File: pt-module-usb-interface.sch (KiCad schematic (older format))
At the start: 9 parts

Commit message: Connected EVERYTHING. Ran ERC. There are still some power errors.
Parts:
- 10k1: renamed from 10k; value R -> 10k1
- 27R1, 27R2: renamed from 27R; value R -> 27R
- 4k1: renamed from 4k7; value R -> 4k1
- gave numbers to parts that had none: 3
- renumbered 47pF to 47pF1, 47pF to 47pF2
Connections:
- no-connect marks 1 -> 5
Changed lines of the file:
@@
 LIBS:ftdi
 LIBS:relays
+LIBS:microchip_dspic33dsc
+LIBS:microchip_pic10mcu
+LIBS:microchip_pic12mcu
+LIBS:microchip_pic16mcu
+LIBS:microchip_pic18mcu
+LIBS:microchip_pic24mcu
+LIBS:microchip_pic32mcu
 LIBS:pt-module-cache
 EELAYER 25 0
@@
 $Descr A4 11693 8268
 encoding utf-8
-Sheet 8 13
+Sheet 7 13
 Title ""
 Date ""
@@
 $EndDescr
 $Comp
-L USB_OTG J?
+L USB_OTG J8
 U 1 1 59836C96
 P 3800 4850
-F 0 "J?" H 3600 5300 50  0000 L CNN
+F 0 "J8" H 3600 5300 50  0000 L CNN
 F 1 "USB_OTG" H 3600 5200 50  0000 L CNN
 F 2 "" H 3950 4800 50  0001 C CNN
@@
 $EndComp
 $Comp
-L R 4k7
+L R 4k1
 U 1 1 59836D8F
 P 5400 4900
-F 0 "4k7" V 5480 4900 50  0000 C CNN
-F 1 "R" V 5400 4900 50  0000 C CNN
+F 0 "4k1" V 5480 4900 50  0000 C CNN
+F 1 "4k1" V 5400 4900 50  0000 C CNN
 F 2 "" V 5330 4900 50  0001 C CNN
 F 3 "" H 5400 4900 50  0001 C CNN
@@
 $EndComp
 $Comp
-L R 10k
+L R 10k1
 U 1 1 59836DF0
 P 5400 5350
-F 0 "10k" V 5480 5350 50  0000 C CNN
-F 1 "R" V 5400 5350 50  0000 C CNN
+F 0 "10k1" V 5480 5350 50  0000 C CNN
+F 1 "10k1" V 5400 5350 50  0000 C CNN
 F 2 "" V 5330 5350 50  0001 C CNN
 F 3 "" H 5400 5350 50  0001 C CNN
@@
 $EndComp
 $Comp
-L GND #PWR055
+L GND #PWR062
 U 1 1 59837539
 P 5400 5650
-F 0 "#PWR055" H 5400 5400 50  0001 C CNN
+F 0 "#PWR062" H 5400 5400 50  0001 C CNN
 F 1 "GND" H 5400 5500 50  0000 C CNN
 F 2 "" H 5400 5650 50  0001 C CNN
@@
 $EndComp
 $Comp
-L GND #PWR056
+L GND #PWR063
 U 1 1 59837659
 P 3800 5400
-F 0 "#PWR056" H 3800 5150 50  0001 C CNN
+F 0 "#PWR063" H 3800 5150 50  0001 C CNN
 F 1 "GND" H 3800 5250 50  0000 C CNN
 F 2 "" H 3800 5400 50  0001 C CNN
@@
 NoConn ~ 4100 5050
 $Comp
-L +3.3V #PWR057
+L +3.3V #PWR064
 U 1 1 59837A65
 P 5650 1750
-F 0 "#PWR057" H 5650 1600 50  0001 C CNN
+F 0 "#PWR064" H 5650 1600 50  0001 C CNN
 F 1 "+3.3V" H 5650 1890 50  0000 C CNN
 F 2 "" H 5650 1750 50  0001 C CNN
@@
 $EndComp
 $Comp
-L R 27R
+L R 27R1
 U 1 1 59837D1B
 P 4700 2650
-F 0 "27R" V 4780 2650 50  0000 C CNN
-F 1 "R" V 4700 2650 50  0000 C CNN
+F 0 "27R1" V 4780 2650 50  0000 C CNN
+F 1 "27R" V 4700 2650 50  0000 C CNN
 F 2 "" V 4630 2650 50  0001 C CNN
 F 3 "" H 4700 2650 50  0001 C CNN
@@
 $EndComp
 $Comp
-L R 27R
+L R 27R2
 U 1 1 59838172
 P 4700 2750
-F 0 "27R" V 4780 2750 50  0000 C CNN
-F 1 "R" V 4700 2750 50  0000 C CNN
+F 0 "27R2" V 4780 2750 50  0000 C CNN
+F 1 "27R" V 4700 2750 50  0000 C CNN
 F 2 "" V 4630 2750 50  0001 C CNN
 F 3 "" H 4700 2750 50  0001 C CNN
@@
 $EndComp
 $Comp
-L C_Small 47pF
+L C_Small 47pF1
 U 1 1 59838B31
 P 4700 3450
-F 0 "47pF" H 4710 3520 50  0000 L CNN
+F 0 "47pF1" H 4710 3520 50  0000 L CNN
 F 1 "C_Small" H 4710 3370 50  0000 L CNN
 F 2 "" H 4700 3450 50  0001 C CNN
@@
 $EndComp
 $Comp
-L C_Small 47pF
+L C_Small 47pF2
 U 1 1 59838B9F
 P 4700 3750
-F 0 "47pF" H 4710 3820 50  0000 L CNN
+F 0 "47pF2" H 4710 3820 50  0000 L CNN
 F 1 "C_Small" H 4710 3670 50  0000 L CNN
 F 2 "" H 4700 3750 50  0001 C CNN
@@
 $EndComp
 $Comp
-L GND #PWR058
+L GND #PWR065
 U 1 1 59838D4F
 P 4800 3600
-F 0 "#PWR058" H 4800 3350 50  0001 C CNN
+F 0 "#PWR065" H 4800 3350 50  0001 C CNN
 F 1 "GND" H 4800 3450 50  0000 C CNN
 F 2 "" H 4800 3600 50  0001 C CNN
@@
 $EndComp
 $Comp
-L FT230XS U?
+L FT230XS U8
 U 1 1 59839565
 P 5750 2750
-F 0 "U?" H 5200 3350 50  0000 L CNN
+F 0 "U8" H 5200 3350 50  0000 L CNN
 F 1 "FT230XS" H 6050 3350 50  0000 L CNN
 F 2 "SSOP-16" H 5750 2750 50  0001 C CNN
@@
 $EndComp
 $Comp
-L C_Small C?
+L C_Small C13
 U 1 1 59839A23
 P 4950 3200
-F 0 "C?" H 4960 3270 50  0000 L CNN
+F 0 "C13" H 4960 3270 50  0000 L CNN
 F 1 "C_Small" H 4960 3120 50  0000 L CNN
 F 2 "" H 4950 3200 50  0001 C CNN
@@
 	1    0    0    -1
 $EndComp
-Wire Wire Line
-	5400 5500 5400 5650
-Wire Wire Line
-	3800 5250 3800 5400
-Wire Wire Line
-	5650 1750 5650 2050
-Wire Wire Line
-	5050 2650 4850 2650
-Wire Wire Line
-	5050 2750 4850 2750
-Wire Wire Line
-	4100 4950 4300 4950
-Wire Wire Line
-	4300 4950 4300 2650
-Wire Wire Line
-	4300 2650 4550 2650
-Wire Wire Line
-	4100 4850 4450 4850
-Wire Wire Line
-	4450 4850 4450 2750
-Wire Wire Line
-	4450 2750 4550 2750
-Wire Wire Line
-	4600 3450 4300 3450
-Connection ~ 4300 3450
-Wire Wire Line
-	4600 3750 4450 3750
-Connection ~ 4450 3750
-Wire Wire Line
-	4800 3450 4800 3750
-Connection ~ 4800 3600
-Wire Wire Line
-	4950 1950 5850 1950
-Wire Wire Line
-	4950 1950 4950 3100
-Wire Wire Line
-	4950 2350 5050 2350
-Wire Wire Line
-	4950 2950 5050 2950
-Connection ~ 4950 2350
-Wire Wire Line
-	5850 1950 5850 2050
-Wire Wire Line
-	6450 2850 6550 2850
-Wire Wire Line
-	6550 2850 6550 5150
-Connection ~ 4950 2950
-Wire Wire Line
-	4950 3300 4950 3500
-Wire Wire Line
-	4950 3500 5850 3500
-Wire Wire Line
-	5650 3500 5650 3450
-Wire Wire Line
-	5850 3500 5850 3450
-Connection ~ 5650 3500
-$Comp
-L GND #PWR059
+$Comp
+L GND #PWR066
 U 1 1 59839F17
 P 5650 3500
-F 0 "#PWR059" H 5650 3250 50  0001 C CNN
+F 0 "#PWR066" H 5650 3250 50  0001 C CNN
 F 1 "GND" H 5650 3350 50  0000 C CNN
 F 2 "" H 5650 3500 50  0001 C CNN
@@
 	1    0    0    -1
 $EndComp
-Wire Wire Line
-	5400 4750 5400 4650
-Wire Wire Line
-	5400 5200 5400 5050
 Text HLabel 6450 2350 2    60   Input ~ 0
 USB_UART_TXD
@@
 Text HLabel 6450 2650 2    60   Input ~ 0
 USB_UART_CTS
+NoConn ~ 6450 2950
+NoConn ~ 6450 3050
+NoConn ~ 6450 3150
+Wire Wire Line
+	5400 5500 5400 5650
+Wire Wire Line
+	3800 5250 3800 5400
+Wire Wire Line
+	5650 1750 5650 2050
+Wire Wire Line
+	5050 2650 4850 2650
+Wire Wire Line
+	5050 2750 4850 2750
+Wire Wire Line
+	4100 4950 4300 4950
+Wire Wire Line
+	4300 4950 4300 2650
+Wire Wire Line
+	4300 2650 4550 2650
+Wire Wire Line
+	4100 4850 4450 4850
+Wire Wire Line
+	4450 4850 4450 2750
+Wire Wire Line
+	4450 2750 4550 2750
+Wire Wire Line
+	4600 3450 4300 3450
+Connection ~ 4300 3450
+Wire Wire Line
+	4600 3750 4450 3750
+Connection ~ 4450 3750
+Wire Wire Line
+	4800 3450 4800 3750
+Connection ~ 4800 3600
+Wire Wire Line
+	4950 1950 5850 1950
+Wire Wire Line
+	4950 1950 4950 3100
+Wire Wire Line
+	4950 2350 5050 2350
+Wire Wire Line
+	4950 2950 5050 2950
+Connection ~ 4950 2350
+Wire Wire Line
+	5850 1950 5850 2050
+Wire Wire Line
+	6450 2850 6550 2850
+Wire Wire Line
+	6550 2850 6550 5150
+Connection ~ 4950 2950
+Wire Wire Line
+	4950 3300 4950 3500
+Wire Wire Line
+	4950 3500 5850 3500
+Wire Wire Line
+	5650 3500 5650 3450
+Wire Wire Line
+	5850 3500 5850 3450
+Connection ~ 5650 3500
+Wire Wire Line
+	5400 4750 5400 4650
+Wire Wire Line
+	5400 5200 5400 5050
 Wire Wire Line
 	5400 4650 4100 4650
@@
 Connection ~ 5400 5150
 Connection ~ 5650 1950
+NoConn ~ 3700 5250
 $EndSCHEMATC

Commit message: USB interface fix
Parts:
- C13: renamed from 47pF1; value C_Small -> 47pF
- C14: renamed from 47pF2; value C_Small -> 47pF
- C15: renamed from C13; value C_Small -> 100nF
- R17: renamed from 4k1; value 4k1 -> 4k7
- R18: renamed from 10k1; value 10k1 -> 10k
- renumbered 27R1 to R15, 27R2 to R16
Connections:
- net +3V3: no longer C15.1, U8.10 (3V3OUT), U8.11 (~RESET), U8.3 (VCCIO)
- net at J8.1 (VBUS): now also R17.2; no longer R17.1
- net at C13.2, J8.2 (D-): now also R15.1; no longer R15.2
- net at C14.2, J8.3 (D+): now also R16.1; no longer R16.2
- net at R18.1, U8.15 (CBUS0): now also R17.1; no longer R17.2
- net at U8.9 (USBDM): now also R15.2; no longer R15.1
- net at U8.8 (USBDP): now also R16.2; no longer R16.1
- new net: C15.1, U8.10 (3V3OUT), U8.11 (~RESET), U8.3 (VCCIO)
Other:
- moved on the sheet: J8, R15, R16, R17, R18
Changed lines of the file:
@@
 L USB_OTG J8
 U 1 1 59836C96
-P 3800 4850
-F 0 "J8" H 3600 5300 50  0000 L CNN
-F 1 "USB_OTG" H 3600 5200 50  0000 L CNN
-F 2 "" H 3950 4800 50  0001 C CNN
-F 3 "" H 3950 4800 50  0001 C CNN
-	1    3800 4850
-	1    0    0    -1
-$EndComp
-$Comp
-L R 4k1
+P 3800 4200
+F 0 "J8" H 3600 4650 50  0000 L CNN
+F 1 "USB_OTG" H 3600 4550 50  0000 L CNN
+F 2 "" H 3950 4150 50  0001 C CNN
+F 3 "" H 3950 4150 50  0001 C CNN
+	1    3800 4200
+	1    0    0    -1
+$EndComp
+$Comp
+L R R17
 U 1 1 59836D8F
-P 5400 4900
-F 0 "4k1" V 5480 4900 50  0000 C CNN
-F 1 "4k1" V 5400 4900 50  0000 C CNN
-F 2 "" V 5330 4900 50  0001 C CNN
-F 3 "" H 5400 4900 50  0001 C CNN
-	1    5400 4900
-	1    0    0    -1
-$EndComp
-$Comp
-L R 10k1
+P 5600 4000
+F 0 "R17" V 5680 4000 50  0000 C CNN
+F 1 "4k7" V 5600 4000 50  0000 C CNN
+F 2 "" V 5530 4000 50  0001 C CNN
+F 3 "" H 5600 4000 50  0001 C CNN
+	1    5600 4000
+	0    1    1    0
+$EndComp
+$Comp
+L R R18
 U 1 1 59836DF0
-P 5400 5350
-F 0 "10k1" V 5480 5350 50  0000 C CNN
-F 1 "10k1" V 5400 5350 50  0000 C CNN
-F 2 "" V 5330 5350 50  0001 C CNN
-F 3 "" H 5400 5350 50  0001 C CNN
-	1    5400 5350
-	1    0    0    -1
-$EndComp
-$Comp
-L GND #PWR062
+P 5900 4200
+F 0 "R18" V 5980 4200 50  0000 C CNN
+F 1 "10k" V 5900 4200 50  0000 C CNN
+F 2 "" V 5830 4200 50  0001 C CNN
+F 3 "" H 5900 4200 50  0001 C CNN
+	1    5900 4200
+	1    0    0    -1
+$EndComp
+$Comp
+L GND #PWR62
 U 1 1 59837539
-P 5400 5650
-F 0 "#PWR062" H 5400 5400 50  0001 C CNN
-F 1 "GND" H 5400 5500 50  0000 C CNN
-F 2 "" H 5400 5650 50  0001 C CNN
-F 3 "" H 5400 5650 50  0001 C CNN
-	1    5400 5650
-	1    0    0    -1
-$EndComp
-$Comp
-L GND #PWR063
+P 5900 4500
+F 0 "#PWR62" H 5900 4250 50  0001 C CNN
+F 1 "GND" H 5900 4350 50  0000 C CNN
+F 2 "" H 5900 4500 50  0001 C CNN
+F 3 "" H 5900 4500 50  0001 C CNN
+	1    5900 4500
+	1    0    0    -1
+$EndComp
+$Comp
+L GND #PWR58
 U 1 1 59837659
-P 3800 5400
-F 0 "#PWR063" H 3800 5150 50  0001 C CNN
-F 1 "GND" H 3800 5250 50  0000 C CNN
-F 2 "" H 3800 5400 50  0001 C CNN
-F 3 "" H 3800 5400 50  0001 C CNN
-	1    3800 5400
-	1    0    0    -1
-$EndComp
-NoConn ~ 4100 5050
-$Comp
-L +3.3V #PWR064
+P 3800 4750
+F 0 "#PWR58" H 3800 4500 50  0001 C CNN
+F 1 "GND" H 3800 4600 50  0000 C CNN
+F 2 "" H 3800 4750 50  0001 C CNN
+F 3 "" H 3800 4750 50  0001 C CNN
+	1    3800 4750
+	1    0    0    -1
+$EndComp
+NoConn ~ 4100 4400
+$Comp
+L +3.3V #PWR60
 U 1 1 59837A65
 P 5650 1750
-F 0 "#PWR064" H 5650 1600 50  0001 C CNN
+F 0 "#PWR60" H 5650 1600 50  0001 C CNN
 F 1 "+3.3V" H 5650 1890 50  0000 C CNN
 F 2 "" H 5650 1750 50  0001 C CNN
@@
 $EndComp
 $Comp
-L R 27R1
+L R R15
 U 1 1 59837D1B
-P 4700 2650
-F 0 "27R1" V 4780 2650 50  0000 C CNN
-F 1 "27R" V 4700 2650 50  0000 C CNN
-F 2 "" V 4630 2650 50  0001 C CNN
-F 3 "" H 4700 2650 50  0001 C CNN
-	1    4700 2650
-	0    1    1    0
-$EndComp
-$Comp
-L R 27R2
+P 4300 3000
+F 0 "R15" V 4380 3000 50  0000 C CNN
+F 1 "27R" V 4300 3000 50  0000 C CNN
+F 2 "" V 4230 3000 50  0001 C CNN
+F 3 "" H 4300 3000 50  0001 C CNN
+	1    4300 3000
+	-1   0    0    1
+$EndComp
+$Comp
+L R R16
 U 1 1 59838172
-P 4700 2750
-F 0 "27R2" V 4780 2750 50  0000 C CNN
-F 1 "27R" V 4700 2750 50  0000 C CNN
-F 2 "" V 4630 2750 50  0001 C CNN
-F 3 "" H 4700 2750 50  0001 C CNN
-	1    4700 2750
-	0    1    1    0
-$EndComp
-$Comp
-L C_Small 47pF1
+P 4500 3000
+F 0 "R16" V 4580 3000 50  0000 C CNN
+F 1 "27R" V 4500 3000 50  0000 C CNN
+F 2 "" V 4430 3000 50  0001 C CNN
+F 3 "" H 4500 3000 50  0001 C CNN
+	1    4500 3000
+	-1   0    0    1
+$EndComp
+$Comp
+L C_Small C13
 U 1 1 59838B31
 P 4700 3450
-F 0 "47pF1" H 4710 3520 50  0000 L CNN
-F 1 "C_Small" H 4710 3370 50  0000 L CNN
+F 0 "C13" H 4710 3520 50  0000 L CNN
+F 1 "47pF" H 4710 3370 50  0000 L CNN
 F 2 "" H 4700 3450 50  0001 C CNN
 F 3 "" H 4700 3450 50  0001 C CNN
@@
 $EndComp
 $Comp
-L C_Small 47pF2
+L C_Small C14
 U 1 1 59838B9F
 P 4700 3750
-F 0 "47pF2" H 4710 3820 50  0000 L CNN
-F 1 "C_Small" H 4710 3670 50  0000 L CNN
+F 0 "C14" H 4710 3820 50  0000 L CNN
+F 1 "47pF" H 4710 3670 50  0000 L CNN
 F 2 "" H 4700 3750 50  0001 C CNN
 F 3 "" H 4700 3750 50  0001 C CNN
@@
 $EndComp
 $Comp
-L GND #PWR065
+L GND #PWR59
 U 1 1 59838D4F
 P 4800 3600
-F 0 "#PWR065" H 4800 3350 50  0001 C CNN
+F 0 "#PWR59" H 4800 3350 50  0001 C CNN
 F 1 "GND" H 4800 3450 50  0000 C CNN
 F 2 "" H 4800 3600 50  0001 C CNN
@@
 $EndComp
 $Comp
-L C_Small C13
+L C_Small C15
 U 1 1 59839A23
 P 4950 3200
-F 0 "C13" H 4960 3270 50  0000 L CNN
-F 1 "C_Small" H 4960 3120 50  0000 L CNN
+F 0 "C15" H 4960 3270 50  0000 L CNN
+F 1 "100nF" H 4960 3120 50  0000 L CNN
 F 2 "" H 4950 3200 50  0001 C CNN
 F 3 "" H 4950 3200 50  0001 C CNN
@@
 $EndComp
 $Comp
-L GND #PWR066
+L GND #PWR61
 U 1 1 59839F17
 P 5650 3500
-F 0 "#PWR066" H 5650 3250 50  0001 C CNN
+F 0 "#PWR61" H 5650 3250 50  0001 C CNN
 F 1 "GND" H 5650 3350 50  0000 C CNN
 F 2 "" H 5650 3500 50  0001 C CNN
@@
 NoConn ~ 6450 3050
 NoConn ~ 6450 3150
-Wire Wire Line
-	5400 5500 5400 5650
-Wire Wire Line
-	3800 5250 3800 5400
-Wire Wire Line
-	5650 1750 5650 2050
-Wire Wire Line
-	5050 2650 4850 2650
-Wire Wire Line
-	5050 2750 4850 2750
-Wire Wire Line
-	4100 4950 4300 4950
-Wire Wire Line
-	4300 4950 4300 2650
-Wire Wire Line
-	4300 2650 4550 2650
-Wire Wire Line
-	4100 4850 4450 4850
-Wire Wire Line
-	4450 4850 4450 2750
-Wire Wire Line
-	4450 2750 4550 2750
-Wire Wire Line
-	4600 3450 4300 3450
-Connection ~ 4300 3450
-Wire Wire Line
-	4600 3750 4450 3750
-Connection ~ 4450 3750
+NoConn ~ 3700 4600
+Wire Wire Line
+	5900 4350 5900 4500
+Wire Wire Line
+	3800 4600 3800 4750
+Wire Wire Line
+	4500 2750 5050 2750
+Wire Wire Line
+	4500 4200 4100 4200
 Wire Wire Line
 	4800 3450 4800 3750
@@
 Wire Wire Line
 	6450 2850 6550 2850
-Wire Wire Line
-	6550 2850 6550 5150
 Connection ~ 4950 2950
 Wire Wire Line
@@
 Connection ~ 5650 3500
 Wire Wire Line
-	5400 4750 5400 4650
-Wire Wire Line
-	5400 5200 5400 5050
-Wire Wire Line
-	5400 4650 4100 4650
-Wire Wire Line
-	6550 5150 5400 5150
-Connection ~ 5400 5150
-Connection ~ 5650 1950
-NoConn ~ 3700 5250
+	4100 4000 5450 4000
+Wire Wire Line
+	5650 2050 5650 1750
+Wire Wire Line
+	6550 2850 6550 4000
+Wire Wire Line
+	6550 4000 5750 4000
+Wire Wire Line
+	5900 4050 5900 4000
+Connection ~ 5900 4000
+Wire Wire Line
+	4300 4300 4100 4300
+Wire Wire Line
+	4500 2750 4500 2850
+Wire Wire Line
+	4500 3150 4500 4200
+Connection ~ 4500 3750
+Wire Wire Line
+	4600 3750 4500 3750
+Wire Wire Line
+	5050 2650 4300 2650
+Wire Wire Line
+	4300 2650 4300 2850
+Wire Wire Line
+	4300 3150 4300 4300
+Wire Wire Line
+	4300 3450 4600 3450
+Connection ~ 4300 3450
 $EndSCHEMATC

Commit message: Re-annotation
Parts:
- renumbered C13 to C11, C14 to C12, C15 to C13, R15 to R13, R16 to R14, R17 to R15, R18 to R16, U8 to U7
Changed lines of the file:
@@
 $EndComp
 $Comp
-L R R17
+L R R15
 U 1 1 59836D8F
 P 5600 4000
-F 0 "R17" V 5680 4000 50  0000 C CNN
+F 0 "R15" V 5680 4000 50  0000 C CNN
 F 1 "4k7" V 5600 4000 50  0000 C CNN
 F 2 "" V 5530 4000 50  0001 C CNN
@@
 $EndComp
 $Comp
-L R R18
+L R R16
 U 1 1 59836DF0
 P 5900 4200
-F 0 "R18" V 5980 4200 50  0000 C CNN
+F 0 "R16" V 5980 4200 50  0000 C CNN
 F 1 "10k" V 5900 4200 50  0000 C CNN
 F 2 "" V 5830 4200 50  0001 C CNN
@@
 $EndComp
 $Comp
-L GND #PWR62
+L GND #PWR59
 U 1 1 59837539
 P 5900 4500
-F 0 "#PWR62" H 5900 4250 50  0001 C CNN
+F 0 "#PWR59" H 5900 4250 50  0001 C CNN
 F 1 "GND" H 5900 4350 50  0000 C CNN
 F 2 "" H 5900 4500 50  0001 C CNN
@@
 $EndComp
 $Comp
-L GND #PWR58
+L GND #PWR55
 U 1 1 59837659
 P 3800 4750
-F 0 "#PWR58" H 3800 4500 50  0001 C CNN
+F 0 "#PWR55" H 3800 4500 50  0001 C CNN
 F 1 "GND" H 3800 4600 50  0000 C CNN
 F 2 "" H 3800 4750 50  0001 C CNN
@@
 NoConn ~ 4100 4400
 $Comp
-L +3.3V #PWR60
+L +3.3V #PWR57
 U 1 1 59837A65
 P 5650 1750
-F 0 "#PWR60" H 5650 1600 50  0001 C CNN
+F 0 "#PWR57" H 5650 1600 50  0001 C CNN
 F 1 "+3.3V" H 5650 1890 50  0000 C CNN
 F 2 "" H 5650 1750 50  0001 C CNN
@@
 $EndComp
 $Comp
-L R R15
+L R R13
 U 1 1 59837D1B
 P 4300 3000
-F 0 "R15" V 4380 3000 50  0000 C CNN
+F 0 "R13" V 4380 3000 50  0000 C CNN
 F 1 "27R" V 4300 3000 50  0000 C CNN
 F 2 "" V 4230 3000 50  0001 C CNN
@@
 $EndComp
 $Comp
-L R R16
+L R R14
 U 1 1 59838172
 P 4500 3000
-F 0 "R16" V 4580 3000 50  0000 C CNN
+F 0 "R14" V 4580 3000 50  0000 C CNN
 F 1 "27R" V 4500 3000 50  0000 C CNN
 F 2 "" V 4430 3000 50  0001 C CNN
@@
 $EndComp
 $Comp
-L C_Small C13
+L C_Small C11
 U 1 1 59838B31
 P 4700 3450
-F 0 "C13" H 4710 3520 50  0000 L CNN
+F 0 "C11" H 4710 3520 50  0000 L CNN
 F 1 "47pF" H 4710 3370 50  0000 L CNN
 F 2 "" H 4700 3450 50  0001 C CNN
@@
 $EndComp
 $Comp
-L C_Small C14
+L C_Small C12
 U 1 1 59838B9F
 P 4700 3750
-F 0 "C14" H 4710 3820 50  0000 L CNN
+F 0 "C12" H 4710 3820 50  0000 L CNN
 F 1 "47pF" H 4710 3670 50  0000 L CNN
 F 2 "" H 4700 3750 50  0001 C CNN
@@
 $EndComp
 $Comp
-L GND #PWR59
+L GND #PWR56
 U 1 1 59838D4F
 P 4800 3600
-F 0 "#PWR59" H 4800 3350 50  0001 C CNN
+F 0 "#PWR56" H 4800 3350 50  0001 C CNN
 F 1 "GND" H 4800 3450 50  0000 C CNN
 F 2 "" H 4800 3600 50  0001 C CNN
@@
 $EndComp
 $Comp
-L FT230XS U8
+L FT230XS U7
 U 1 1 59839565
 P 5750 2750
-F 0 "U8" H 5200 3350 50  0000 L CNN
+F 0 "U7" H 5200 3350 50  0000 L CNN
 F 1 "FT230XS" H 6050 3350 50  0000 L CNN
 F 2 "SSOP-16" H 5750 2750 50  0001 C CNN
@@
 $EndComp
 $Comp
-L C_Small C15
+L C_Small C13
 U 1 1 59839A23
 P 4950 3200
-F 0 "C15" H 4960 3270 50  0000 L CNN
+F 0 "C13" H 4960 3270 50  0000 L CNN
 F 1 "100nF" H 4960 3120 50  0000 L CNN
 F 2 "" H 4950 3200 50  0001 C CNN
@@
 $EndComp
 $Comp
-L GND #PWR61
+L GND #PWR58
 U 1 1 59839F17
 P 5650 3500
-F 0 "#PWR61" H 5650 3250 50  0001 C CNN
+F 0 "#PWR58" H 5650 3250 50  0001 C CNN
 F 1 "GND" H 5650 3350 50  0000 C CNN
 F 2 "" H 5650 3500 50  0001 C CNN

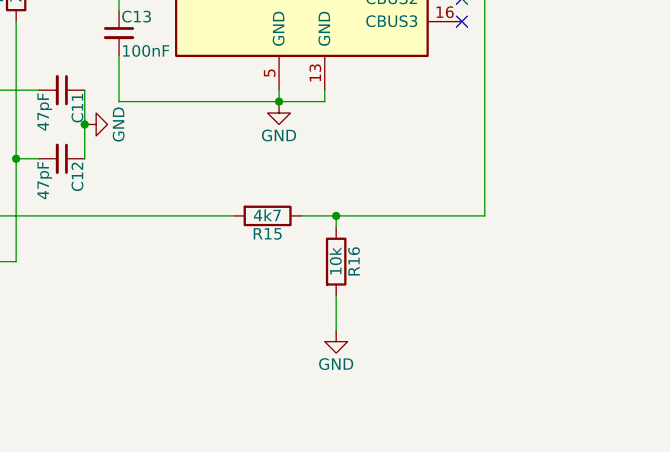
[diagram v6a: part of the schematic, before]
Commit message: Added power flags and ERC error count shrinked into 3.
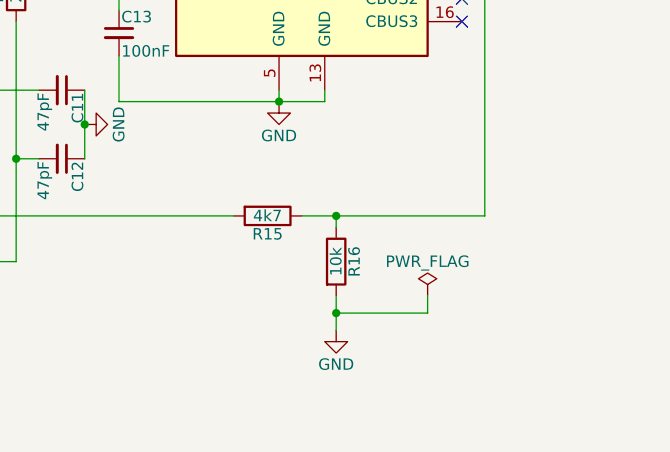
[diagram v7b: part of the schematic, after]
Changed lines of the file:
@@
 $EndComp
 $Comp
-L GND #PWR59
+L GND #PWR058
 U 1 1 59837539
 P 5900 4500
-F 0 "#PWR59" H 5900 4250 50  0001 C CNN
+F 0 "#PWR058" H 5900 4250 50  0001 C CNN
 F 1 "GND" H 5900 4350 50  0000 C CNN
 F 2 "" H 5900 4500 50  0001 C CNN
@@
 $EndComp
 $Comp
-L GND #PWR55
+L GND #PWR059
 U 1 1 59837659
 P 3800 4750
-F 0 "#PWR55" H 3800 4500 50  0001 C CNN
+F 0 "#PWR059" H 3800 4500 50  0001 C CNN
 F 1 "GND" H 3800 4600 50  0000 C CNN
 F 2 "" H 3800 4750 50  0001 C CNN
@@
 NoConn ~ 4100 4400
 $Comp
-L +3.3V #PWR57
+L +3.3V #PWR060
 U 1 1 59837A65
 P 5650 1750
-F 0 "#PWR57" H 5650 1600 50  0001 C CNN
+F 0 "#PWR060" H 5650 1600 50  0001 C CNN
 F 1 "+3.3V" H 5650 1890 50  0000 C CNN
 F 2 "" H 5650 1750 50  0001 C CNN
@@
 $EndComp
 $Comp
-L GND #PWR56
+L GND #PWR061
 U 1 1 59838D4F
 P 4800 3600
-F 0 "#PWR56" H 4800 3350 50  0001 C CNN
+F 0 "#PWR061" H 4800 3350 50  0001 C CNN
 F 1 "GND" H 4800 3450 50  0000 C CNN
 F 2 "" H 4800 3600 50  0001 C CNN
@@
 $EndComp
 $Comp
-L GND #PWR58
+L GND #PWR062
 U 1 1 59839F17
 P 5650 3500
-F 0 "#PWR58" H 5650 3250 50  0001 C CNN
+F 0 "#PWR062" H 5650 3250 50  0001 C CNN
 F 1 "GND" H 5650 3350 50  0000 C CNN
 F 2 "" H 5650 3500 50  0001 C CNN
@@
 NoConn ~ 6450 3150
 NoConn ~ 3700 4600
+$Comp
+L PWR_FLAG #FLG063
+U 1 1 599577D8
+P 6300 4350
+F 0 "#FLG063" H 6300 4425 50  0001 C CNN
+F 1 "PWR_FLAG" H 6300 4500 50  0000 C CNN
+F 2 "" H 6300 4350 50  0001 C CNN
+F 3 "" H 6300 4350 50  0001 C CNN
+	1    6300 4350
+	1    0    0    -1
+$EndComp
 Wire Wire Line
 	5900 4350 5900 4500
@@
 	4300 3450 4600 3450
 Connection ~ 4300 3450
+Wire Wire Line
+	6300 4350 6300 4425
+Wire Wire Line
+	6300 4425 5900 4425
+Connection ~ 5900 4425
 $EndSCHEMATC
